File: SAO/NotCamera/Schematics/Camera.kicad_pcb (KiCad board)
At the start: 2 copper layers, 38.1 x 21 mm, 14 parts, among them J1 Conn_02x03_Odd_Even, Q1 Q_PNP_BCE, Q2 Q_PNP_BCE

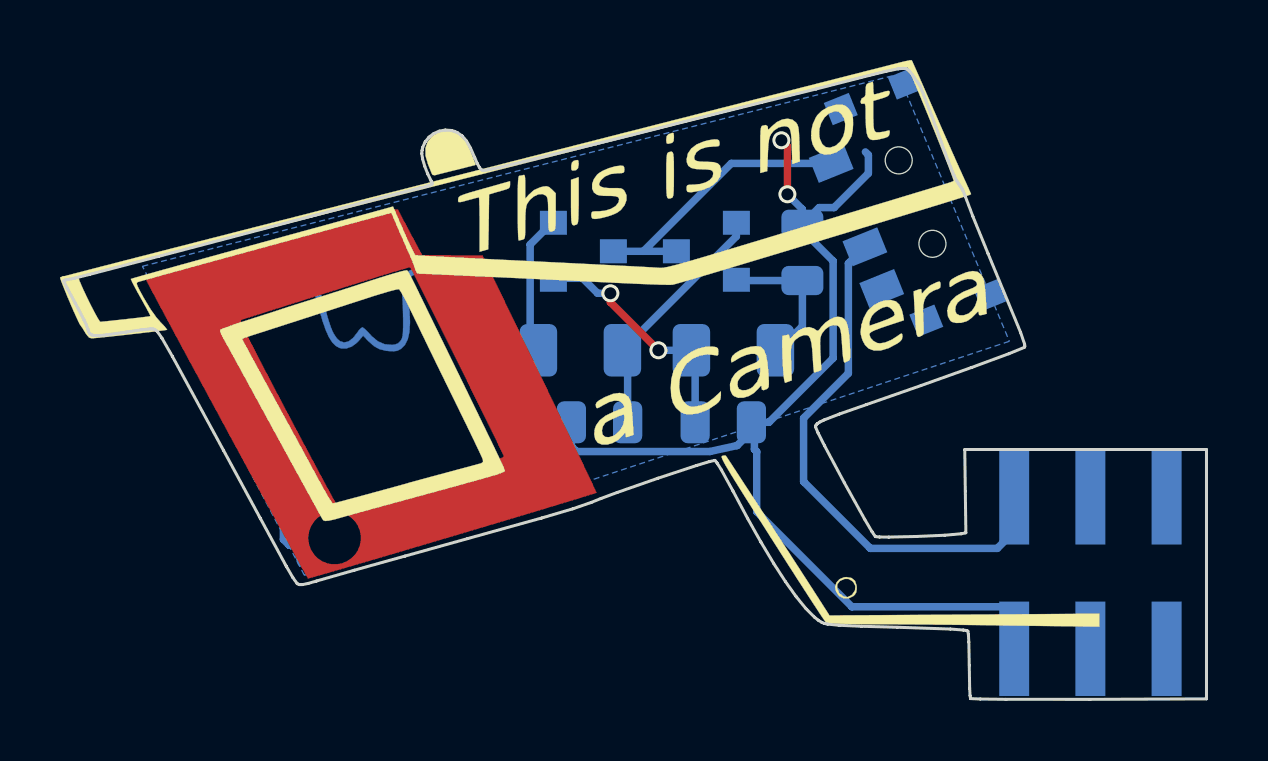
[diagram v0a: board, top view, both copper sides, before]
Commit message: Making stencils
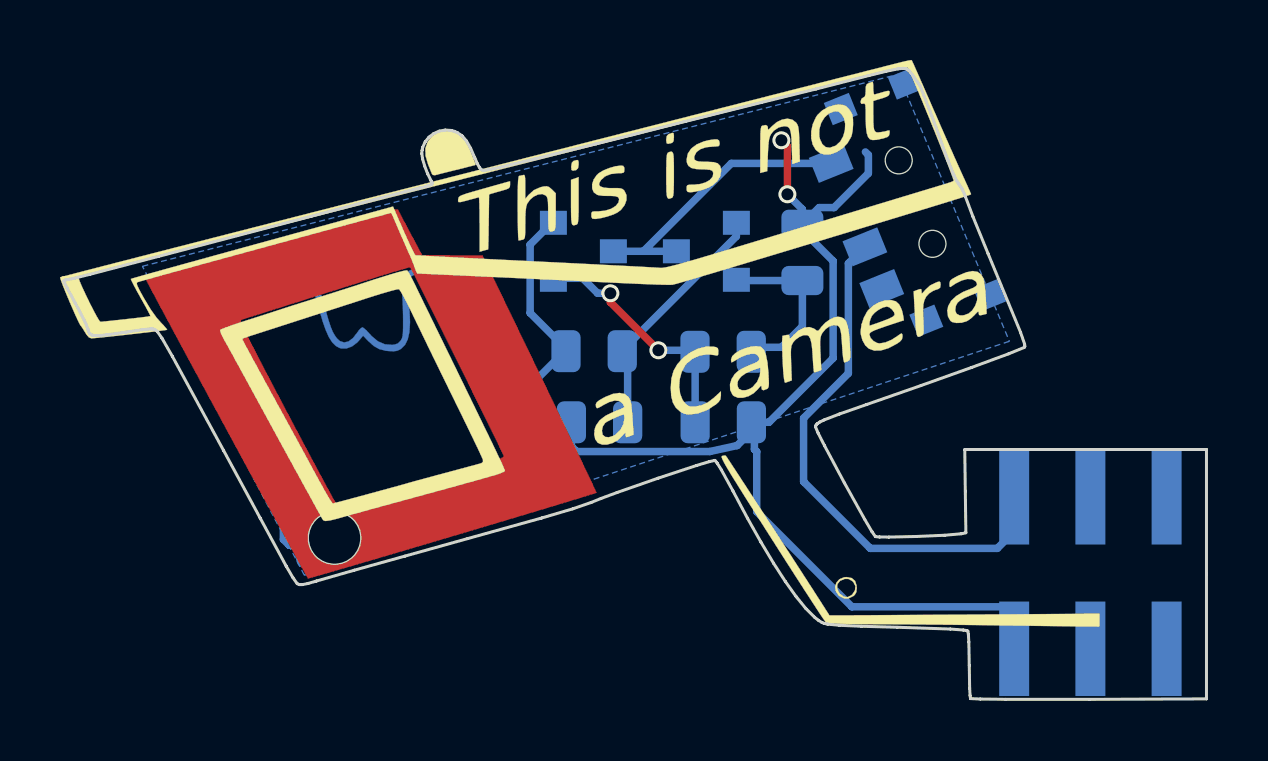
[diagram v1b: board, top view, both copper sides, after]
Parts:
- C1, C2: footprint Capacitor_SMD:C_1206_3216Metric -> Capacitor_SMD:C_0805_2012Metric
- moved C1 0.46 mm to (146.1, 107.7)
- moved C2 0.35 mm to (150.4, 107.8)
- renumbered ON-> to SW1
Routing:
- net Net-(C2-Pad1): track 4.83 -> 5.86 mm
- net Net-(C1-Pad1): track 10.3 -> 11.0 mm
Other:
- board text removed: "_|"
